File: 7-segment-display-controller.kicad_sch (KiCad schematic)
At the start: 55 parts, among them J101 Tag Connector, J102 USB_B_Micro, J103 JST 2.54 Header, J104 JST 2.54 Header, J105 JST 2.54 Header, J106 JST 2.54 Header, J107 Conn_01x02, Q101 AO3501A, SW101 SW_DIP_x04, SW106 SW_Push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

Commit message: switch MCU to STM32F401
- switch MCU to STM32F401 because STM32F303 does not have DMA stream
- add EEPROM
- removed D+ pull-up resistor
- switch status LED to blue, changed resistor values
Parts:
- removed C110: 1uF, Capacitor_SMD:C_0603_1608Metric, symbol Device:C_Small
- removed R108: 1K5, Resistor_SMD:R_0603_1608Metric, symbol Device:R_Small
- removed U101: STM32F303CBT6, Package_QFP:LQFP-48_7x7mm_P0.5mm, symbol MCU_ST_STM32F3:STM32F303CBTx
- added C111: 100nF, Capacitor_SMD:C_0603_1608Metric, symbol Device:C_Small
- added C202: 4.7uF, Capacitor_SMD:C_0603_1608Metric, symbol Device:C_Small
- added U101: STM32F401RCTx, Package_QFP:LQFP-64_10x10mm_P0.5mm, symbol MCU_ST_STM32F4:STM32F401RCTx
- added U104: M24C64-RMN, Package_SO:SOIC-8_3.9x4.9mm_P1.27mm, symbol Memory_EEPROM:M24C02-RMN
- C106: value 10nF -> 100nF; LCSC C57112 -> C14663
- D107: value GREEN -> BLUE; LCSC C72043 -> C72041
- H101, H102, H103, H104: now left out of the parts list
- J107: footprint Connector_JST:JST_XH_B2B-XH-A_1x02_P2.50mm_Vertical -> Connector_JST:JST_PH_B2B-PH-K_1x02_P2.00mm_Vertical
- R101, R105: value 1K5 -> 2K2; LCSC C22843 -> C4190
- R103: value 47 -> 0; LCSC C23182 -> C21189
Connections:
- net +3.3VA: now also U101.13 (VREF+)
- net +3V3: now also C111.1, U101.19 (VDD), U101.32 (VDD), U101.48 (VDD), U101.64 (VDD), U104.8 (VCC)
- net BOOT0: now also U101.60 (BOOT0)
- net DIP1: now also U101.53 (PC12)
- net DIP2: now also U101.52 (PC11)
- net DIP3: now also U101.51 (PC10)
- net D_N: now also U101.44 (PA11)
- net D_P: now also U101.45 (PA12)
- net GND: now also C111.2, C202.2, U101.12 (VSSA), U101.18 (VSS), U101.31 (VSS), U101.47 (VSS), U101.63 (VSS), U104.1 (E0), U104.2 (E1), U104.3 (E2), U104.4 (VSS)
- net HSE_IN: now also U101.5 (PH0)
- net HSE_OUT: now also U101.6 (PH1)
- net IR_RECV: now also U101.20 (PA4)
- net LED_HB: now also U101.23 (PA7)
- net LED_UI: now also U101.21 (PA5)
- net LSE_IN: now also U101.3 (PC14)
- net LSE_OUT: now also U101.4 (PC15)
- net NRST: now also D104.3 (K), U101.7 (NRST); no longer D104.1 (K)
- net RGB_LED: now also U101.22 (PA6)
- net SCL: now also U101.58 (PB6), U104.6 (SCL)
- net SDA: now also U101.59 (PB7), U104.5 (SDA)
- net SWCLK: now also U101.49 (PA14)
- net SWDIO: now also U101.46 (PA13)
- net SWO: now also D104.1 (K), U101.55 (PB3); no longer D104.3 (K)
- net UART_RX: now also U101.17 (PA3)
- net UART_TX: now also U101.16 (PA2)
- net VBAT: now also U101.1 (VBAT)
- net VBUS: no longer J101.1 (Pin_1)
- net ~{OE}: now also U101.28 (PB2)
- new net: C202.1, U101.30 (VCAP1)
- new net ~{EEPROM}: U101.33 (PB12), U104.7 (~{WC})
- no-connect marks 18 -> 31
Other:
- note added: "64Kbit EEPROM"
- note added: "NRST is internally pulled-up. Pull to ground to reset. BOOT0 Pin Selection: 0 = Load from main flash memory 1 = Programming via UART/USB Use DIP to change program settings."
- note removed: "USB D+ line must be externally pulled up with 3V3 with 1.5KΩ. NRST is internally pulled-up. Pull to ground to reset. BOOT0 Pin Selection: 0 = Load from main flash memory 1 = Programming via UART/USB Use DIP to change program settings."
- moved on the sheet: C103, C104, C105, C106, C107, C202, D104, FB101, R109, R110, Y103

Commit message: update BOM
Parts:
- J107, OLED101: now left out of the parts list
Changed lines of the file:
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@@
   )
   (symbol (lib_id "Connector_Generic:Conn_01x02") (at 76.2 46.99 180) (unit 1)
-    (in_bom yes) (on_board yes) (dnp no)
+    (in_bom no) (on_board yes) (dnp no)
     (property "Reference" "J107" (at 76.2 41.91 0)
       (effects (font (size 1.27 1.27)))
@@
   )
   (symbol (lib_id "User Symbols:OLED_I2C") (at 33.02 80.01 0) (unit 1)
-    (in_bom yes) (on_board yes) (dnp no)
+    (in_bom no) (on_board yes) (dnp no)
     (property "Reference" "OLED101" (at 29.21 69.85 0)
       (effects (font (size 1.27 1.27)) (justify left))
@@
       (effects (font (size 1.27 1.27)) hide)
     )
+    (property "LCSC" "" (at 33.02 80.01 0)
+      (effects (font (size 1.27 1.27)) hide)
+    )

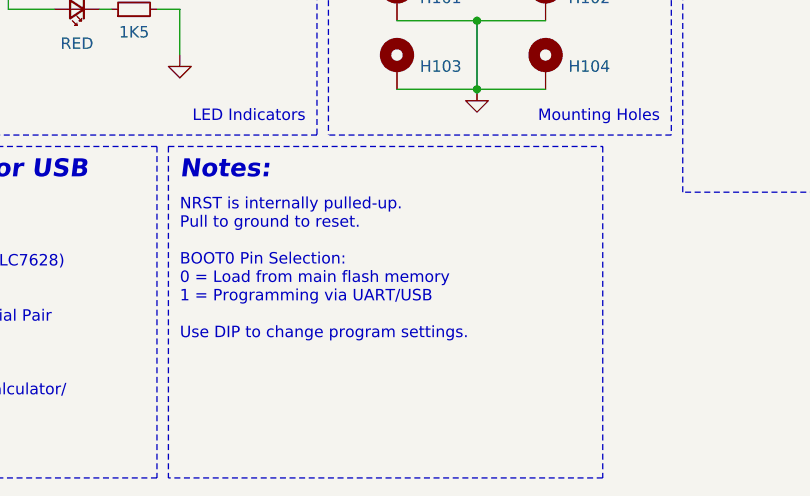
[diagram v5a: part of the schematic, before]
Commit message: update net color and schematic notes
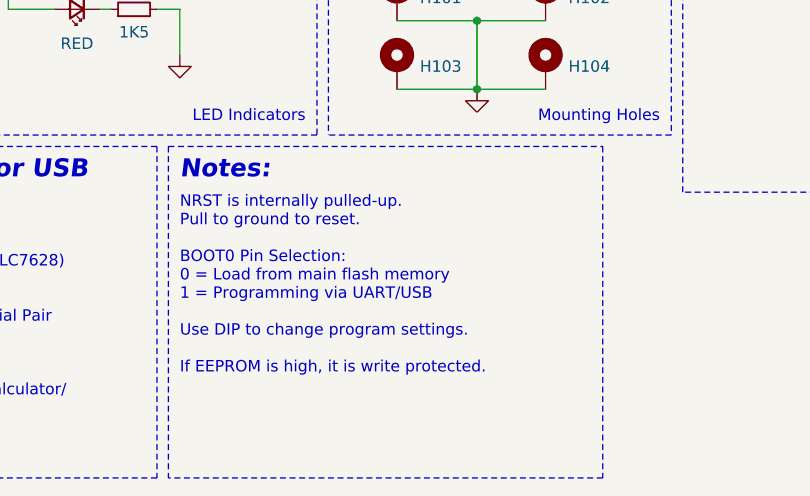
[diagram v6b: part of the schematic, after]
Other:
- note added: "NRST is internally pulled-up. Pull to ground to reset. BOOT0 Pin Selection: 0 = Load from main flash memory 1 = Programming via UART/USB Use DIP to change program settings. If EEPROM is high, it is write protected."
- note removed: "NRST is internally pulled-up. Pull to ground to reset. BOOT0 Pin Selection: 0 = Load from main flash memory 1 = Programming via UART/USB Use DIP to change program settings."
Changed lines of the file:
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@@
     (effects (font (size 1.27 1.27)) (justify right bottom))
   )
-  (text "NRST is internally pulled-up.\nPull to ground to reset.\n\nBOOT0 Pin Selection:\n0 = Load from main flash memory\n1 = Programming via UART/USB\n\nUse DIP to change program settings."
-    (at 128.27 181.61 0)
+  (text "NRST is internally pulled-up.\nPull to ground to reset.\n\nBOOT0 Pin Selection:\n0 = Load from main flash memory\n1 = Programming via UART/USB\n\nUse DIP to change program settings.\n\nIf EEPROM is high, it is write protected."
+    (at 128.27 185.42 0)
     (effects (font (size 1.27 1.27)) (justify left bottom))
   )
